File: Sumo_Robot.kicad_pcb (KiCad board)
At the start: 2 copper layers, 4 parts

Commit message: started layout of Rev A
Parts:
- added D1: LED, LED_SMD:LED_1210_3225Metric, F.Cu at (-53.6, 79.5)
- added D2: LED, LED_SMD:LED_1210_3225Metric, F.Cu at (-53.6, 83.8)
- added D3: LED, LED_SMD:LED_1210_3225Metric, F.Cu at (-46.4, 96.5)
- added D4: LED, LED_SMD:LED_1210_3225Metric, F.Cu at (-65.3, 90.1)
- added D5: LED, LED_SMD:LED_1210_3225Metric, F.Cu at (-65.3, 94.4)
- added D6: LED, LED_SMD:LED_1210_3225Metric, F.Cu at (-65.3, 98.7)
- added D7: LED, LED_SMD:LED_1210_3225Metric, F.Cu at (-65.3, 103.0)
- added D8: LED, LED_SMD:LED_1210_3225Metric, F.Cu at (-50.9, 32.9)
- added H1: MountingHole, MountingHole:MountingHole_6.4mm_M6, F.Cu at (-60.9, 16.8)
- added H2: MountingHole, MountingHole:MountingHole_6.4mm_M6, F.Cu at (-60.9, 31.2)
- added H3: MountingHole, MountingHole:MountingHole_6.4mm_M6, F.Cu at (-60.9, 45.5)
- added H4: MountingHole, MountingHole:MountingHole_6.4mm_M6, F.Cu at (-60.9, 59.9)
- added J2: Screw_Terminal_01x04, TerminalBlock:TerminalBlock_Altech_AK300-4_P5.00mm, F.Cu at (105.9, 67.0)
- added J3: Screw_Terminal_01x04, TerminalBlock:TerminalBlock_Altech_AK300-4_P5.00mm, F.Cu at (187.0, 67.5)
- added J4: Screw_Terminal_01x04, TerminalBlock:TerminalBlock_Altech_AK300-4_P5.00mm, F.Cu at (-105.8, 51.5)
- added J5: Screw_Terminal_01x04, TerminalBlock:TerminalBlock_Altech_AK300-4_P5.00mm, F.Cu at (-105.8, 71.0)
- added J6: Screw_Terminal_01x04, TerminalBlock:TerminalBlock_Altech_AK300-4_P5.00mm, F.Cu at (-105.8, 90.5)
- added R1: 3k, Resistor_SMD:R_1210_3225Metric, F.Cu at (-48.0, 79.5)
- added R10: 1k, Resistor_SMD:R_1210_3225Metric, F.Cu at (-51.0, 16.0)
- added R11: 10k, Resistor_SMD:R_1210_3225Metric, F.Cu at (-51.0, 20.2)
- added R12: 10k, Resistor_SMD:R_1210_3225Metric, F.Cu at (-51.0, 24.4)
- added R13: 1k, Resistor_SMD:R_1210_3225Metric, F.Cu at (-51.0, 28.6)
- added R2: 1k, Resistor_SMD:R_1210_3225Metric, F.Cu at (-48.0, 83.7)
- added R3: 10k, Resistor_SMD:R_1210_3225Metric, F.Cu at (-52.0, 90.1)
- added R4: 1k, Resistor_SMD:R_1210_3225Metric, F.Cu at (-52.0, 94.3)
- added R5: 1k, Resistor_SMD:R_1210_3225Metric, F.Cu at (-59.7, 90.1)
- added R6: 1k, Resistor_SMD:R_1210_3225Metric, F.Cu at (-59.7, 94.3)
- added R7: 1k, Resistor_SMD:R_1210_3225Metric, F.Cu at (-59.7, 98.5)
- added R8: 1k, Resistor_SMD:R_1210_3225Metric, F.Cu at (-59.7, 102.7)
- added R9: 47k, Resistor_SMD:R_1210_3225Metric, F.Cu at (-51.0, 11.8)
- added SW1: SW_SPST, Button_Switch_SMD:SW_MEC_5GSH9, F.Cu at (-62.3, 77.4)
- added U5: AMS1117-3.3, Package_TO_SOT_SMD:SOT-223-3_TabPin2, F.Cu at (-51.5, 73.3)
- added U6: TSOP38233, OptoDevice:Vishay_MINICAST-3Pin, F.Cu at (-47.6, 90.1)
- moved H2 61.5 mm to (248.5, 31.0)
- moved H4 55.7 mm to (245.5, 124.5)
- moved H1 27.1 mm to (34.5, 32.5)

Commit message: added all footprints and step files to components
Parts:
- removed the H1 at (-60.9, 16.8)
- removed the H1 at (34.5, 32.5)
- removed the H2 at (248.5, 31.0)
- removed the H2 at (-60.9, 31.2)
- removed the H3 at (57.0, 134.5)
- removed the H3 at (-60.9, 45.5)
- removed the H4 at (-60.9, 59.9)
- removed the H4 at (245.5, 124.5)
- added C1: 10uf, Capacitor_SMD:C_1210_3225Metric, F.Cu at (-161.1, 21.7)
- added C10: 1uf, Capacitor_SMD:C_1210_3225Metric, F.Cu at (-47.7, -34.8)
- added C11: 10uf, Capacitor_SMD:C_1210_3225Metric, F.Cu at (-178.1, -70.8)
- added C12: 100nf, Capacitor_SMD:C_1210_3225Metric, F.Cu at (-178.1, -66.6)
- added C2: 22uf, Capacitor_SMD:C_1210_3225Metric, F.Cu at (-161.6, 31.7)
- added C3: 160pF, Capacitor_SMD:C_1210_3225Metric, F.Cu at (-51.0, -26.8)
- added C4: 0.1uF, Capacitor_SMD:C_1210_3225Metric, F.Cu at (-77.2, -26.7)
- added C5: 10uf, Capacitor_SMD:C_1210_3225Metric, F.Cu at (-77.2, -22.5)
- added C6: 0.1uF, Capacitor_SMD:C_1210_3225Metric, F.Cu at (-77.2, -18.2)
- added C7: 0.1uF, Capacitor_SMD:C_1210_3225Metric, F.Cu at (-77.2, -53.6)
- added C8: 10uf, Capacitor_SMD:C_1210_3225Metric, F.Cu at (-77.2, -49.4)
- added C9: 0.1uF, Capacitor_SMD:C_1210_3225Metric, F.Cu at (-77.2, -45.1)
- added D9: LED, LED_SMD:LED_1210_3225Metric, F.Cu at (-66.0, 103.7)
- added H1: MountingHole, MountingHole:MountingHole_4.5mm_Pad, F.Cu at (-337.1, -51.8)
- added H2: MountingHole, MountingHole:MountingHole_4.5mm_Pad, F.Cu at (-332.6, -35.3)
- added H3: MountingHole, MountingHole:MountingHole_4.5mm_Pad, F.Cu at (-358.6, -42.8)
- added H4: MountingHole, MountingHole:MountingHole_4.5mm_Pad, F.Cu at (-356.6, -19.8)
- added J1: ~, Connector_AMASS:AMASS_XT60-F_1x02_P7.20mm_Vertical, F.Cu at (-207.8, 80.7)
- added J10: Screw_Terminal_01x03, TerminalBlock_Phoenix:TerminalBlock_Phoenix_MKDS-1,5-3_1x03_P5.00mm_Horizontal, F.Cu at (-95.5, -25.2)
- added J11: ~, TerminalBlock_Phoenix:TerminalBlock_Phoenix_MKDS-1,5-2_1x02_P5.00mm_Horizontal, F.Cu at (-76.5, -34.8)
- added J12: Screw_Terminal_01x02, TerminalBlock_Phoenix:TerminalBlock_Phoenix_MKDS-1,5-2_1x02_P5.00mm_Horizontal, F.Cu at (-64.4, -34.8)
- added J13: ~, TerminalBlock_Phoenix:TerminalBlock_Phoenix_MKDS-1,5-2_1x02_P5.00mm_Horizontal, F.Cu at (-76.5, -61.6)
- added J14: Screw_Terminal_01x02, TerminalBlock_Phoenix:TerminalBlock_Phoenix_MKDS-1,5-2_1x02_P5.00mm_Horizontal, F.Cu at (-64.4, -61.6)
- added J15: Conn_01x02, Connector_PinHeader_1.00mm:PinHeader_1x02_P1.00mm_Vertical, F.Cu at (-48.9, -39.5)
- added J16: Conn_01x03, Connector_PinHeader_1.00mm:PinHeader_1x03_P1.00mm_Vertical, F.Cu at (-43.2, -35.4)
- added J17: Conn_01x08, Connector_PinHeader_1.00mm:PinHeader_1x08_P1.00mm_Vertical, F.Cu at (-52.2, -39.5)
- added J18: Conn_01x02, Connector_PinHeader_1.00mm:PinHeader_1x02_P1.00mm_Vertical, F.Cu at (-45.5, -39.5)
- added J19: Conn_01x02, Connector_PinHeader_1.00mm:PinHeader_1x02_P1.00mm_Vertical, F.Cu at (-42.2, -39.5)
- added J7: Screw_Terminal_01x03, TerminalBlock_Phoenix:TerminalBlock_Phoenix_MKDS-1,5-3_1x03_P5.00mm_Horizontal, F.Cu at (-95.5, -61.6)
- added J8: Screw_Terminal_01x03, TerminalBlock_Phoenix:TerminalBlock_Phoenix_MKDS-1,5-3_1x03_P5.00mm_Horizontal, F.Cu at (-95.5, -49.5)
- added J9: Screw_Terminal_01x03, TerminalBlock_Phoenix:TerminalBlock_Phoenix_MKDS-1,5-3_1x03_P5.00mm_Horizontal, F.Cu at (-95.5, -37.4)
- added SW3: SW_Omron_B3FS, Button_Switch_SMD:SW_SPST_Omron_B3FS-100xP, F.Cu at (-148.1, 75.9)
- added U1: ~, Package_SO:TSSOP-28_4.4x9.7mm_P0.65mm, F.Cu at (-101.4, 104.3)
- added U2: ~, Package_SO:SSOP-24_5.3x8.2mm_P0.65mm, F.Cu at (-69.0, -50.7)
- added U3: ~, Package_SO:SSOP-24_5.3x8.2mm_P0.65mm, F.Cu at (-69.0, -23.8)
- added U4: ~, Package_SO:SOP-8_3.76x4.96mm_P1.27mm, F.Cu at (-266.1, 119.3)
- J2, J3, J4, J5, J6: footprint TerminalBlock:TerminalBlock_Altech_AK300-4_P5.00mm -> TerminalBlock_Phoenix:TerminalBlock_Phoenix_MKDS-1,5-4_1x04_P5.00mm_Horizontal
- SW1: footprint Button_Switch_SMD:SW_MEC_5GSH9 -> Button_Switch_SMD:SW_DIP_SPSTx01_Slide_9.78x4.72mm_W8.61mm_P2.54mm
- U5: footprint Package_TO_SOT_SMD:SOT-223-3_TabPin2 -> Package_TO_SOT_SMD:SOT-223
- moved D4 235.7 mm to (-300.3, 73.3)
- moved D5 235.7 mm to (-300.3, 77.6)
- moved D6 235.7 mm to (-300.3, 81.9)
- moved D7 235.7 mm to (-300.3, 86.2)
- moved D3 235.7 mm to (-281.5, 79.7)
- moved J2 235.7 mm to (-129.1, 50.2)
- moved J4 235.7 mm to (-340.9, 34.7)
- moved J5 235.7 mm to (-340.9, 54.2)
- moved J6 235.7 mm to (-340.9, 73.7)
- moved R10 235.7 mm to (-286.0, -0.84)
- moved R11 235.7 mm to (-286.0, 3.37)
- moved R12 235.7 mm to (-286.0, 7.58)
- moved R13 235.7 mm to (-286.0, 11.8)
- moved R5 235.7 mm to (-294.7, 73.2)
- moved R6 235.7 mm to (-294.7, 77.5)
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
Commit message: continued layout
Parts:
- H1, H2, H3, H4: footprint MountingHole:MountingHole_4.5mm_Pad -> MountingHole:MountingHole_2.5mm_Pad
- moved H4 566.2 mm to (190.9, 124.4)
- moved H3 555.7 mm to (190.9, 40.4)
- moved J4 505.4 mm to (156.9, 121.9)
- moved J6 491.8 mm to (149.9, 42.9), turned to 180 degrees
- moved SW1 491.3 mm to (190.9, 115.1), turned to 90 degrees
- moved U5 475.8 mm to (187.6, 96.4)
- moved D6 471.5 mm to (170.9, 65.2), turned to -90 degrees
- moved D7 471.3 mm to (170.9, 80.8), turned to -90 degrees
- moved J5 469.5 mm to (128.4, 42.9), turned to 180 degrees
- moved D5 469.1 mm to (168.3, 56.8)
- moved R6 469.1 mm to (173.9, 56.7)
- moved H2 467.6 mm to (106.9, 124.4)
- moved R7 465.8 mm to (170.9, 70.9), turned to -90 degrees
- moved R8 465.6 mm to (170.9, 86.4), turned to -90 degrees
- moved D1 459.0 mm to (167.8, 110.0)
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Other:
- board outline added: 90 x 90 mm

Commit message: continuing layout
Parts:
- moved H1 118.8 mm to (190.9, 124.4), turned to 180 degrees
- moved H2 118.8 mm to (190.9, 40.4), turned to 180 degrees
- moved H3 118.8 mm to (106.9, 124.4), turned to 180 degrees
- moved H4 118.7 mm to (107.0, 40.5), turned to 180 degrees
- moved J8 104.2 mm to (114.9, 121.9), turned to 0 degrees
- moved J11 99.2 mm to (188.4, 112.4), turned to 90 degrees
- moved J2 98.4 mm to (172.5, 42.9), turned to 180 degrees
- moved J5 89.0 mm to (169.4, 121.9), turned to 0 degrees
- moved J12 87.2 mm to (188.4, 100.9), turned to 90 degrees
- moved J7 86.4 mm to (131.4, 121.9), turned to 0 degrees
- moved J4 83.6 mm to (129.5, 42.9), turned to 180 degrees
- moved J9 82.6 mm to (109.4, 94.4), turned to -90 degrees
- moved J3 80.5 mm to (151.0, 42.9), turned to 180 degrees
- moved J13 80.2 mm to (188.4, 89.4), turned to 90 degrees
- moved J10 79.5 mm to (109.4, 77.9), turned to -90 degrees
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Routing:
- net +3.3V: track 0.00 -> 5.35 mm
- net ML_A02: track 0.00 -> 1.27 mm
- added copper zone on F.Cu, net +3.3V
- added copper zone on F.Cu, net +BATT
- added copper zone on B.Cu, net GND

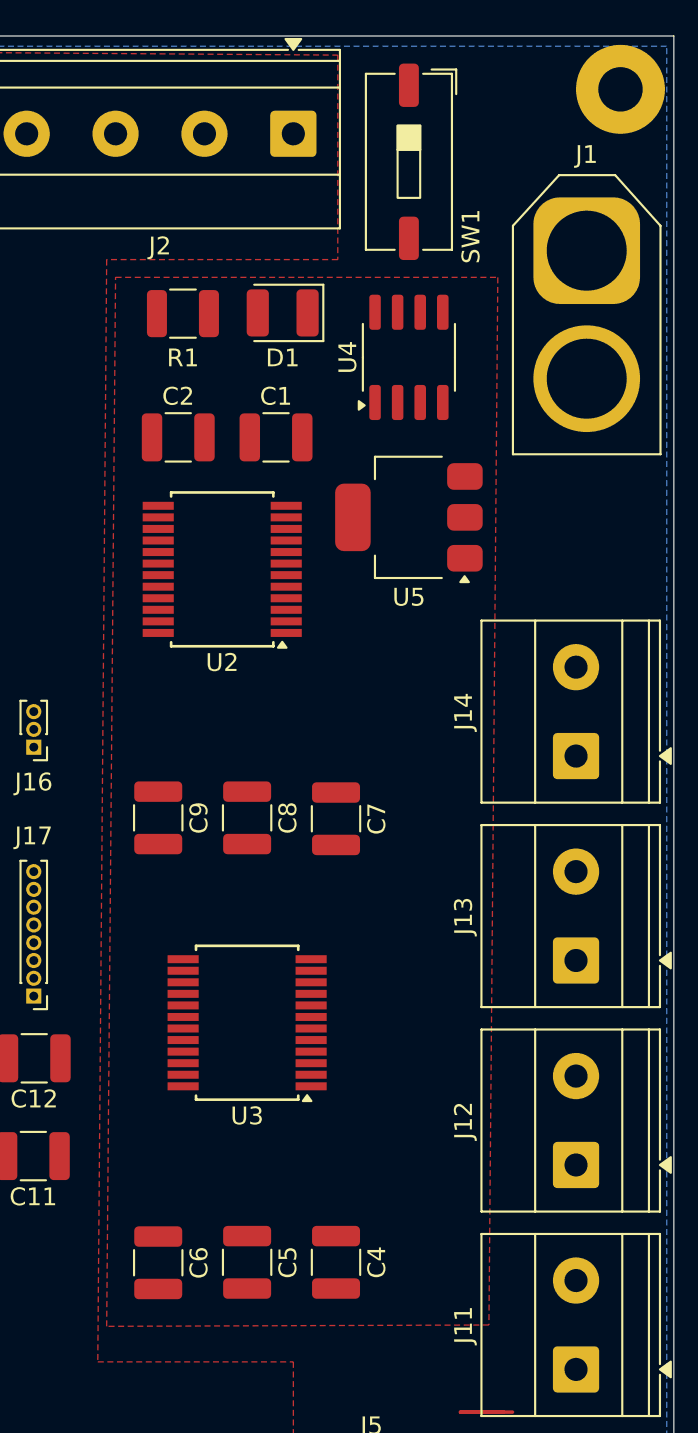
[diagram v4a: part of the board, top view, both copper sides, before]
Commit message: updated infomration on schematic; started working on layout
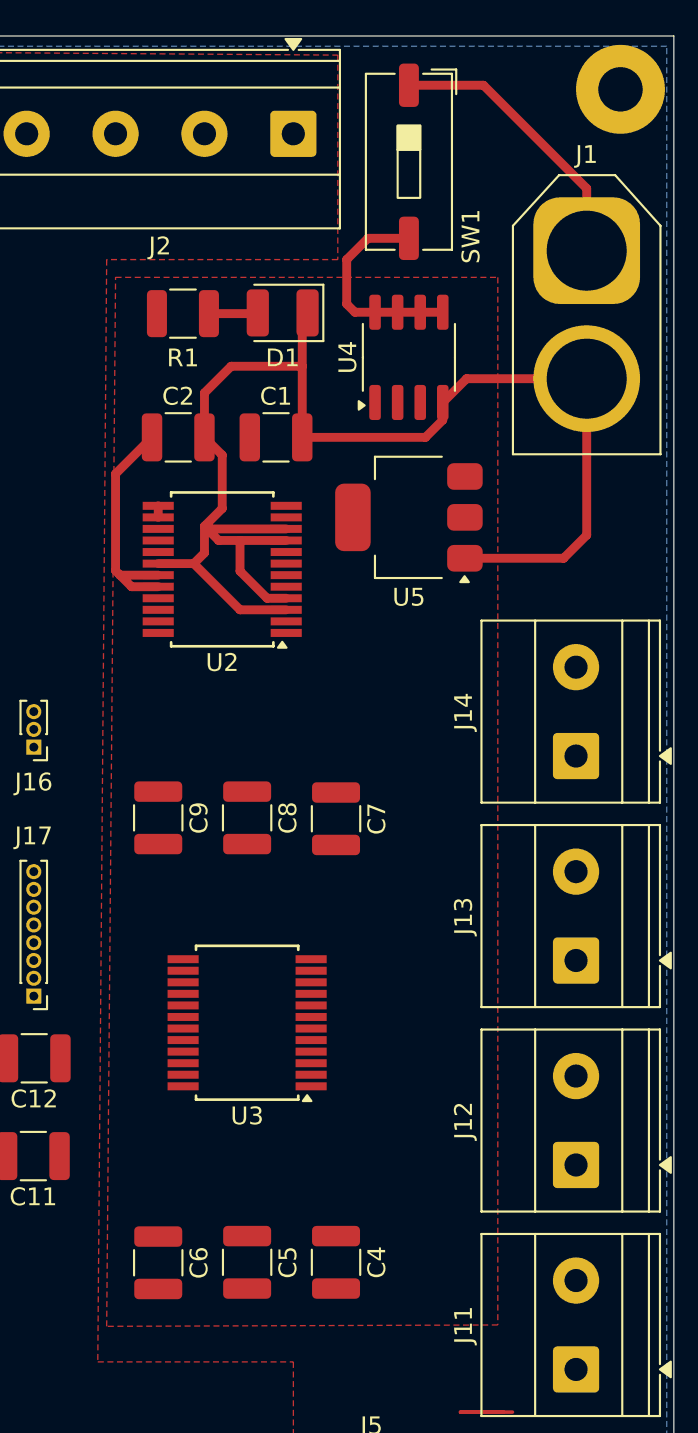
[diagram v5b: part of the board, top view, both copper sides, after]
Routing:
- net GND: track 0.00 -> 80.7 mm
- net Net-(J1-+): track 0.00 -> 15.9 mm
- net +3.3V: track 5.35 -> 18.6 mm
- net Net-(SW1-B): track 0.00 -> 12.1 mm
- net Net-(D1-A): track 0.00 -> 2.76 mm
- net +BATT: track 0.00 -> 0.65 mm

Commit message: layout updates
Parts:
- moved U6 7.05 mm to (120.0, 53.5), turned to -90 degrees
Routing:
- net GND: track 80.7 -> 160.1 mm
- net +3.3V: track 18.6 -> 21.2 mm
- net +BATT: track 0.65 -> 1.60 mm
- net Net-(SW1-B): track 12.1 -> 11.2 mm
- added copper zone on B.Cu, net +3.3V
- added copper zone on F.Cu, net GND
- removed copper zone on F.Cu, net +3.3V
- removed copper zone on B.Cu, net GND

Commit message: Updated PCB Layers and Schematics
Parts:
- moved U5 2.24 mm to (181.0, 65.5)
- moved C10 0.08 mm to (142.4, 67.0)
- moved D8 0.08 mm to (153.5, 67.0)
- moved R13 0.08 mm to (148.0, 67.0)
- turned C11 to 0 degrees
- turned C12 to 0 degrees
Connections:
- U2 pad 10: GND -> unconnected-(U2-PGND2-Pad10)
- U2 pad 12: MR_B01 -> unconnected-(U2-BO1-Pad12)
- U2 pad 2: MR_A01 -> unconnected-(U2-AO1-Pad2)
- U2 pad 4: GND -> unconnected-(U2-PGND1-Pad4)
- U2 pad 6: MR_A02 -> unconnected-(U2-AO2-Pad6)
- U2 pad 8: MR_B02 -> unconnected-(U2-BO2-Pad8)
- U3 pad 10: GND -> unconnected-(U3-PGND2-Pad10)
- U3 pad 12: ML_B01 -> unconnected-(U3-BO1-Pad12)
- U3 pad 2: ML_A01 -> unconnected-(U3-AO1-Pad2)
- U3 pad 4: GND -> unconnected-(U3-PGND1-Pad4)
- U3 pad 6: ML_A02 -> unconnected-(U3-AO2-Pad6)
- U3 pad 8: ML_B02 -> unconnected-(U3-BO2-Pad8)
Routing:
- net GND: track 160.1 -> 102.8 mm, vias 0 -> 8
- net +BATT: track 1.60 -> 45.4 mm, vias 0 -> 9
- net +3.3V: track 21.2 -> 0.00 mm
- net Net-(D5-A): track 0.00 -> 2.80 mm
- net Net-(D4-A): track 0.00 -> 2.76 mm
- net Net-(D7-A): track 0.00 -> 2.75 mm
- net Net-(D6-A): track 0.00 -> 2.75 mm
- net Net-(D2-A): track 0.00 -> 2.70 mm
- net Net-(SW1-B): track 11.2 -> 8.84 mm
- added copper zone on In2.Cu, net (none)
- added copper zone on F.Cu, net +3.3V
- added copper zone on In1.Cu, net +BATT
- added copper zone on B.Cu, net GND
- removed copper zone on B.Cu, net +3.3V
- removed copper zone on F.Cu, net +BATT
- removed copper zone on F.Cu, net GND
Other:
- copper layers 2 -> 4

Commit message: advancing layout
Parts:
- moved D3 10.7 mm to (108.5, 66.6)
- moved U6 8.90 mm to (111.5, 56.0), turned to 0 degrees
- moved R3 8.14 mm to (120.5, 66.5), turned to -90 degrees
- moved R4 4.31 mm to (112.5, 66.5)
- moved C3 1.55 mm to (116.5, 66.5), turned to -90 degrees
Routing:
- net /InfraredReceiver/IR_RECEIVE: track 0.00 -> 88.4 mm, vias 0 -> 2
- net GND: track 102.8 -> 137.4 mm, vias 8 -> 15
- net UNUSED_2: track 0.00 -> 20.7 mm, vias 0 -> 1
- net Net-(U6-Vs): track 0.00 -> 13.1 mm
- net UNUSED_1: track 0.00 -> 11.5 mm, vias 0 -> 1
- net UNUSED_3: track 0.00 -> 7.79 mm
- net UNUSED_5: track 0.00 -> 7.77 mm
- net UNUSED_4: track 0.00 -> 7.64 mm
- net UNUSED_6: track 0.00 -> 7.62 mm
- net UNUSED_7: track 0.00 -> 7.48 mm
- net UNUSED_8: track 0.00 -> 7.33 mm
- net Net-(D3-A): track 0.00 -> 4.00 mm
